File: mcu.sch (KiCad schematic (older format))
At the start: 73 parts, among them J11 RJ45_Shielded, J13 HR911105A, J2 RJ45_Shielded, U3 STM32F207VGT6, U4 MCP2562-E-P, U5 LAN8720A, Y1 Crystal_GND24

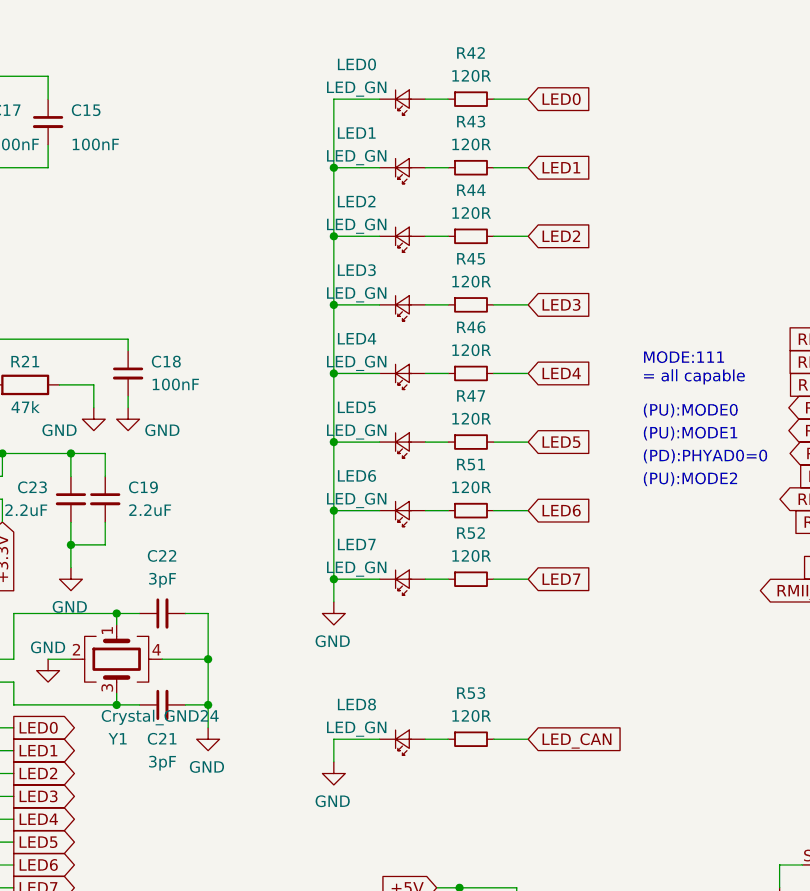
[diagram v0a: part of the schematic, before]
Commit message: added BOM info, minor tweaks to artwork
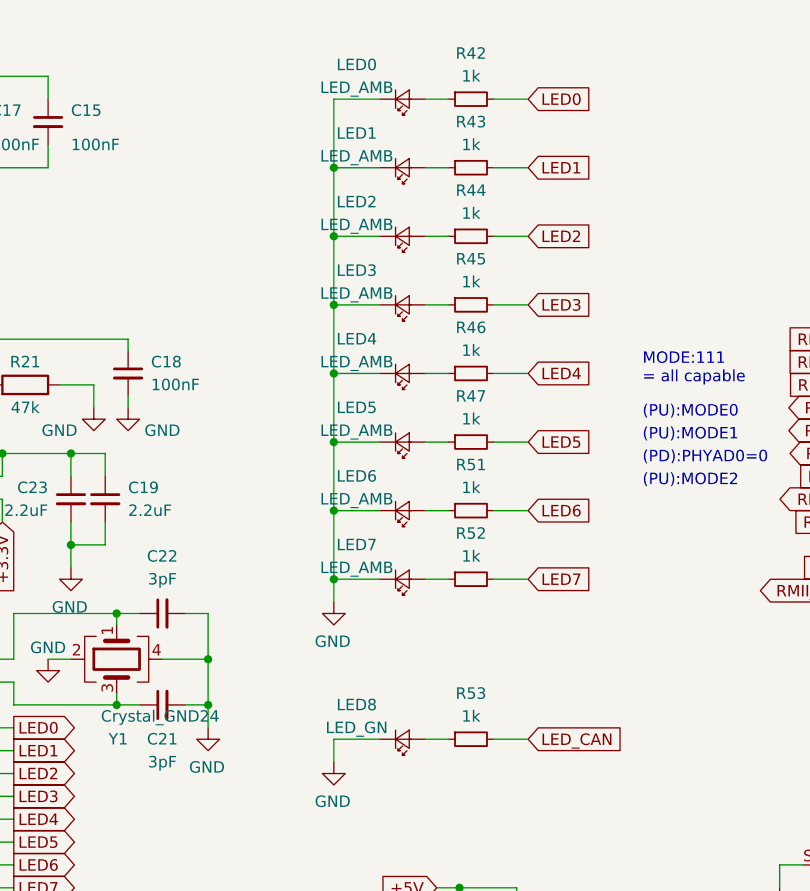
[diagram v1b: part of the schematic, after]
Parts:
- LED0: value LED_GN -> LED_AMB; MPN (none) -> LTST-C190AKT; Mouser (none) -> 859-LTST-C190AKT
- LED1, LED2, LED3, LED4, LED5, LED6, LED7: value LED_GN -> LED_AMB
- R42, R43, R44, R45, R46, R47, R51, R52, R53: value 120R -> 1k
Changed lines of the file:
@@
 P 5250 950
 F 0 "LED0" H 5050 800 50  0000 C CNN
-F 1 "LED_GN" H 5050 900 50  0000 C CNN
+F 1 "LED_AMB" H 5050 900 50  0000 C CNN
 F 2 "LED_SMD:LED_0603_1608Metric_Castellated" V 5250 950 50  0001 C CNN
 F 3 "~" V 5250 950 50  0001 C CNN
+F 4 "LTST-C190AKT" H 5250 950 50  0001 C CNN "MPN"
+F 5 "859-LTST-C190AKT" H 5250 950 50  0001 C CNN "Mouser"
 	1    5250 950
 	1    0    0    1
@@
 AR Path="/5C211FC6/5BE6601F" Ref="R?"  Part="1"
 F 0 "R42" V 5350 950 50  0000 C CNN
-F 1 "120R" V 5450 950 50  0000 C CNN
+F 1 "1k" V 5450 950 50  0000 C CNN
 F 2 "Resistor_SMD:R_0603_1608Metric" H 5550 950 50  0001 C CNN
 F 3 "~" H 5550 950 50  0001 C CNN
@@
 P 5250 1250
 F 0 "LED1" H 5050 1100 50  0000 C CNN
-F 1 "LED_GN" H 5050 1200 50  0000 C CNN
+F 1 "LED_AMB" H 5050 1200 50  0000 C CNN
 F 2 "LED_SMD:LED_0603_1608Metric_Castellated" V 5250 1250 50  0001 C CNN
 F 3 "~" V 5250 1250 50  0001 C CNN
@@
 AR Path="/5C211FC6/5C0171BB" Ref="R?"  Part="1"
 F 0 "R43" V 5350 1250 50  0000 C CNN
-F 1 "120R" V 5450 1250 50  0000 C CNN
+F 1 "1k" V 5450 1250 50  0000 C CNN
 F 2 "Resistor_SMD:R_0603_1608Metric" H 5550 1250 50  0001 C CNN
 F 3 "~" H 5550 1250 50  0001 C CNN
@@
 P 5250 1550
 F 0 "LED2" H 5050 1400 50  0000 C CNN
-F 1 "LED_GN" H 5050 1500 50  0000 C CNN
+F 1 "LED_AMB" H 5050 1500 50  0000 C CNN
 F 2 "LED_SMD:LED_0603_1608Metric_Castellated" V 5250 1550 50  0001 C CNN
 F 3 "~" V 5250 1550 50  0001 C CNN
@@
 AR Path="/5C211FC6/5C036412" Ref="R?"  Part="1"
 F 0 "R44" V 5350 1550 50  0000 C CNN
-F 1 "120R" V 5450 1550 50  0000 C CNN
+F 1 "1k" V 5450 1550 50  0000 C CNN
 F 2 "Resistor_SMD:R_0603_1608Metric" H 5550 1550 50  0001 C CNN
 F 3 "~" H 5550 1550 50  0001 C CNN
@@
 P 5250 1850
 F 0 "LED3" H 5050 1700 50  0000 C CNN
-F 1 "LED_GN" H 5050 1800 50  0000 C CNN
+F 1 "LED_AMB" H 5050 1800 50  0000 C CNN
 F 2 "LED_SMD:LED_0603_1608Metric_Castellated" V 5250 1850 50  0001 C CNN
 F 3 "~" V 5250 1850 50  0001 C CNN
@@
 AR Path="/5C211FC6/5C05605C" Ref="R?"  Part="1"
 F 0 "R45" V 5350 1850 50  0000 C CNN
-F 1 "120R" V 5450 1850 50  0000 C CNN
+F 1 "1k" V 5450 1850 50  0000 C CNN
 F 2 "Resistor_SMD:R_0603_1608Metric" H 5550 1850 50  0001 C CNN
 F 3 "~" H 5550 1850 50  0001 C CNN
@@
 P 5250 2150
 F 0 "LED4" H 5050 2000 50  0000 C CNN
-F 1 "LED_GN" H 5050 2100 50  0000 C CNN
+F 1 "LED_AMB" H 5050 2100 50  0000 C CNN
 F 2 "LED_SMD:LED_0603_1608Metric_Castellated" V 5250 2150 50  0001 C CNN
 F 3 "~" V 5250 2150 50  0001 C CNN
@@
 AR Path="/5C211FC6/5C0760E4" Ref="R?"  Part="1"
 F 0 "R46" V 5350 2150 50  0000 C CNN
-F 1 "120R" V 5450 2150 50  0000 C CNN
+F 1 "1k" V 5450 2150 50  0000 C CNN
 F 2 "Resistor_SMD:R_0603_1608Metric" H 5550 2150 50  0001 C CNN
 F 3 "~" H 5550 2150 50  0001 C CNN
@@
 P 5250 2450
 F 0 "LED5" H 5050 2300 50  0000 C CNN
-F 1 "LED_GN" H 5050 2400 50  0000 C CNN
+F 1 "LED_AMB" H 5050 2400 50  0000 C CNN
 F 2 "LED_SMD:LED_0603_1608Metric_Castellated" V 5250 2450 50  0001 C CNN
 F 3 "~" V 5250 2450 50  0001 C CNN
@@
 AR Path="/5C211FC6/5C0960DF" Ref="R?"  Part="1"
 F 0 "R47" V 5350 2450 50  0000 C CNN
-F 1 "120R" V 5450 2450 50  0000 C CNN
+F 1 "1k" V 5450 2450 50  0000 C CNN
 F 2 "Resistor_SMD:R_0603_1608Metric" H 5550 2450 50  0001 C CNN
 F 3 "~" H 5550 2450 50  0001 C CNN
@@
 P 5250 2750
 F 0 "LED6" H 5050 2600 50  0000 C CNN
-F 1 "LED_GN" H 5050 2700 50  0000 C CNN
+F 1 "LED_AMB" H 5050 2700 50  0000 C CNN
 F 2 "LED_SMD:LED_0603_1608Metric_Castellated" V 5250 2750 50  0001 C CNN
 F 3 "~" V 5250 2750 50  0001 C CNN
@@
 AR Path="/5C211FC6/5C0B676E" Ref="R?"  Part="1"
 F 0 "R51" V 5350 2750 50  0000 C CNN
-F 1 "120R" V 5450 2750 50  0000 C CNN
+F 1 "1k" V 5450 2750 50  0000 C CNN
 F 2 "Resistor_SMD:R_0603_1608Metric" H 5550 2750 50  0001 C CNN
 F 3 "~" H 5550 2750 50  0001 C CNN
@@
 P 5250 3050
 F 0 "LED7" H 5050 2900 50  0000 C CNN
-F 1 "LED_GN" H 5050 3000 50  0000 C CNN
+F 1 "LED_AMB" H 5050 3000 50  0000 C CNN
 F 2 "LED_SMD:LED_0603_1608Metric_Castellated" V 5250 3050 50  0001 C CNN
 F 3 "~" V 5250 3050 50  0001 C CNN
@@
 AR Path="/5C211FC6/5C12EE79" Ref="R?"  Part="1"
 F 0 "R52" V 5350 3050 50  0000 C CNN
-F 1 "120R" V 5450 3050 50  0000 C CNN
+F 1 "1k" V 5450 3050 50  0000 C CNN
 F 2 "Resistor_SMD:R_0603_1608Metric" H 5550 3050 50  0001 C CNN
 F 3 "~" H 5550 3050 50  0001 C CNN
@@
 AR Path="/5C211FC6/5C152FC5" Ref="R?"  Part="1"
 F 0 "R53" V 5350 3750 50  0000 C CNN
-F 1 "120R" V 5450 3750 50  0000 C CNN
+F 1 "1k" V 5450 3750 50  0000 C CNN
 F 2 "Resistor_SMD:R_0603_1608Metric" H 5550 3750 50  0001 C CNN
 F 3 "~" H 5550 3750 50  0001 C CNN

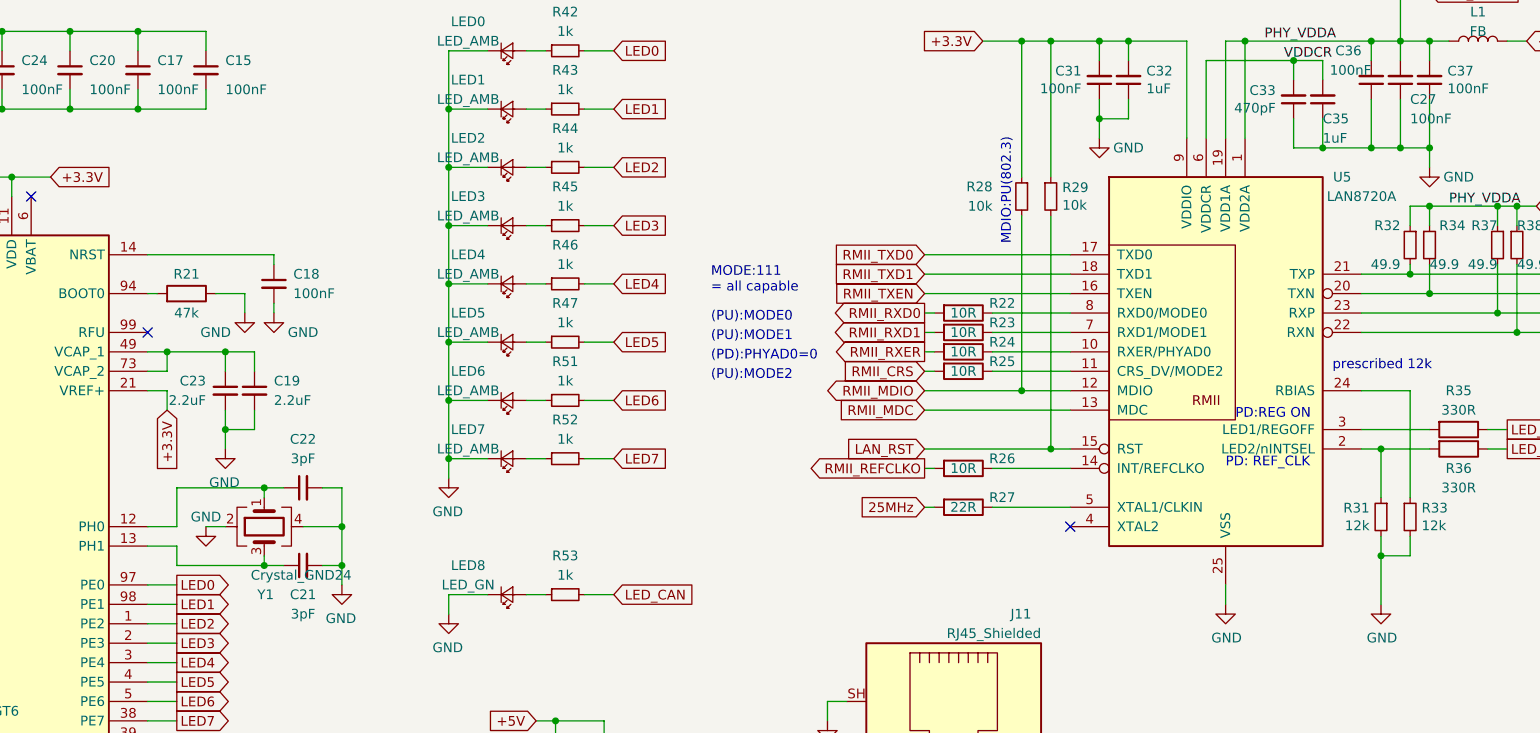
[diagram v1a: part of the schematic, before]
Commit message: adds reset button, some xtal guarding. Schematic reviewed in this version, see https://hackmd.io/-iUjavK_Rz-11sfgLlTnuA# - xtal could be swapped for C_L 10 pF version to reduce susceptibility to environmental factors.
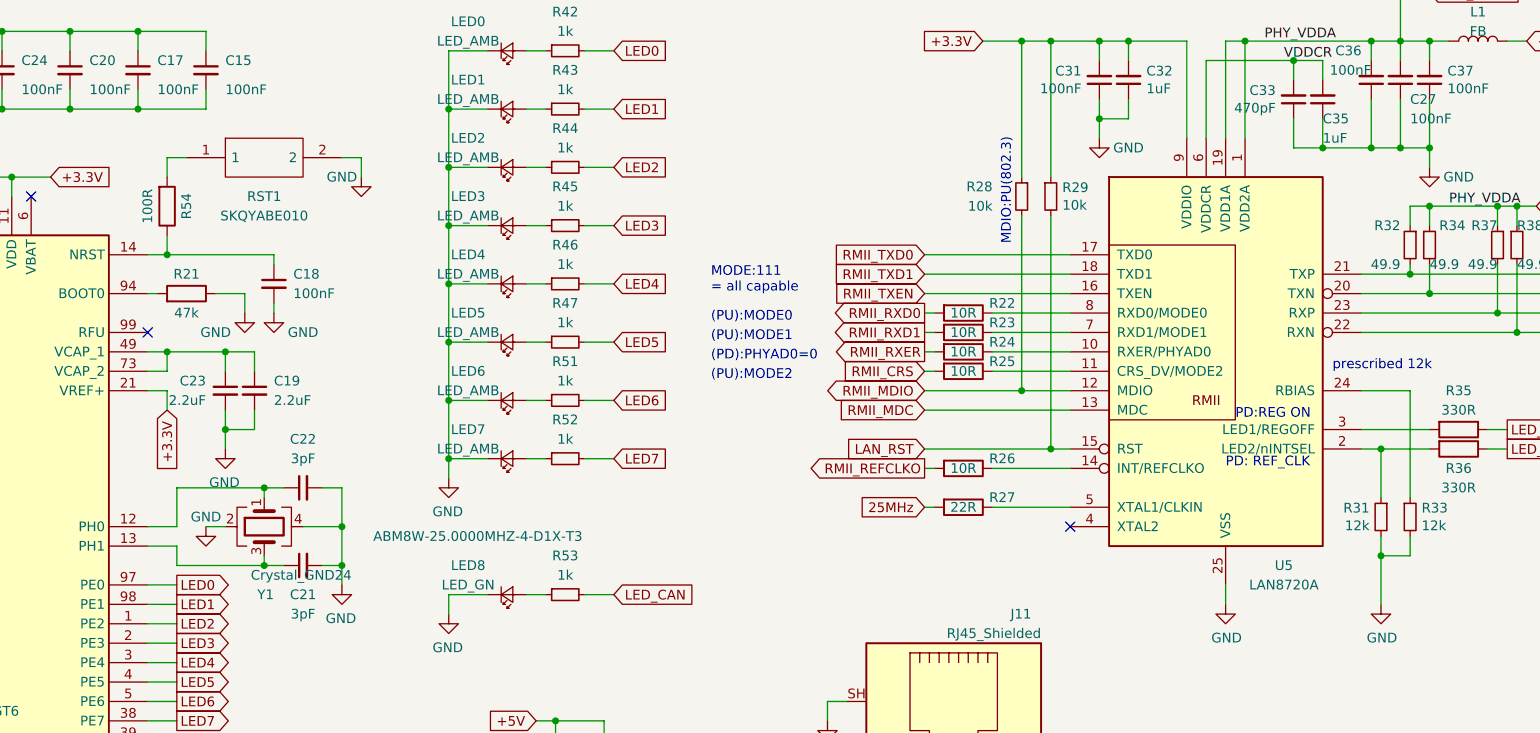
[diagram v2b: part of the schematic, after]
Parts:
- added R54: 100R, Resistor_SMD:R_0603_1608Metric, symbol Device:R
- added RST1: SKQYABE010, SamacSys_Parts:SKQYABE010, symbol SamacSys_Parts:SKQYABE010
- Y1: MPN ABM8-25.000MHZ-10-D1G-T -> ABM8W-25.0000MHZ-4-D1X-T3; Mouser 815-ABM8-25-10-D1G-T -> 815-8W25-4D1XT
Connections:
- net GND: now also RST1.2
- net at C18.1, U3.14 (NRST): now also R54.1
- new net: R54.2, RST1.1
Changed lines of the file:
@@
 AR Path="/5C211DD3/5BBD20DE" Ref="U?"  Part="1"
 AR Path="/5C211FC6/5BBD20DE" Ref="U?"  Part="1"
-F 0 "U5" H 9550 3600 50  0000 C CNN
-F 1 "LAN8720A" H 9650 3500 50  0000 C CNN
+F 0 "U5" H 9250 1600 50  0000 C CNN
+F 1 "LAN8720A" H 9250 1500 50  0000 C CNN
 F 2 "Package_DFN_QFN:QFN-24-1EP_4x4mm_P0.5mm_EP2.6x2.6mm" H 9000 1650 50  0001 L CNN
 F 3 "http://ww1.microchip.com/downloads/en/DeviceDoc/8720a.pdf" H 8750 1650 50  0001 C CNN
@@
 F 2 "Crystal:Crystal_SMD_Abracon_ABM8G-4Pin_3.2x2.5mm" H 4000 3400 50  0001 C CNN
 F 3 "~" H 4000 3400 50  0001 C CNN
-F 4 "ABM8-25.000MHZ-10-D1G-T " V 4000 3400 50  0001 C CNN "MPN"
-F 5 "815-ABM8-25-10-D1G-T " V 4000 3400 50  0001 C CNN "Mouser"
+F 4 "ABM8W-25.0000MHZ-4-D1X-T3" V 4050 2300 50  0000 C CNN "MPN"
+F 5 "815-8W25-4D1XT" V 4000 3400 50  0001 C CNN "Mouser"
 	1    4000 3400
 	0    -1   1    0
@@
 $EndComp
 Wire Wire Line
-	3400 2000 4050 2000
+	3400 2000 3500 2000
 Wire Wire Line
 	4000 3600 4100 3600
@@
 Wire Wire Line
 	9750 5850 9750 5750
+$Comp
+L SamacSys_Parts:SKQYABE010 RST1
+U 1 1 5BE29C94
+P 3600 1500
+F 0 "RST1" H 4000 1300 50  0000 C CNN
+F 1 "SKQYABE010" H 4000 1200 50  0000 C CNN
+F 2 "SamacSys_Parts:SKQYABE010" H 4250 1600 50  0001 L CNN
+F 3 "http://www.alps.com/prod/info/E/HTML/Tact/SurfaceMount/SKQY/SKQYABE010.html#Dimensions" H 4250 1500 50  0001 L CNN
+F 4 "Switch Tactile 6.1 x 3.7 SMT 2.55N Black Button Tactile Switch, SPST-NO 50 mA Surface Mount" H 4250 1400 50  0001 L CNN "Description"
+F 5 "2" H 4250 1300 50  0001 L CNN "Height"
+F 6 "ALPS" H 4250 1200 50  0001 L CNN "Manufacturer_Name"
+F 7 "SKQYABE010" H 4250 1100 50  0001 L CNN "Manufacturer_Part_Number"
+F 8 "9174188" H 4250 1000 50  0001 L CNN "RS Part Number"
+F 9 "http://uk.rs-online.com/web/p/products/9174188" H 4250 900 50  0001 L CNN "RS Price/Stock"
+F 10 "SKQYABE010" H 4250 800 50  0001 L CNN "Arrow Part Number"
+F 11 "https://www.arrow.com/en/products/skqyabe010/alps-electric" H 4250 700 50  0001 L CNN "Arrow Price/Stock"
+F 12 "SKQYABE010" H 3600 1500 50  0001 C CNN "MPN"
+F 13 "688-SKQYAB" H 3600 1500 50  0001 C CNN "Mouser"
+	1    3600 1500
+	1    0    0    -1
+$EndComp
+Connection ~ 3500 2000
+Wire Wire Line
+	3500 2000 4050 2000
+$Comp
+L power:GND #PWR0133
+U 1 1 5BEA740B
+P 4500 1600
+AR Path="/5BBC4BB7/5BEA740B" Ref="#PWR0133"  Part="1"
+AR Path="/5C1EFDBE/5BEA740B" Ref="#PWR?"  Part="1"
+AR Path="/5C211DD3/5BEA740B" Ref="#PWR?"  Part="1"
+AR Path="/5C211FC6/5BEA740B" Ref="#PWR?"  Part="1"
+F 0 "#PWR0133" H 4500 1350 50  0001 C CNN
+F 1 "GND" H 4600 1600 50  0000 C CNN
+F 2 "" H 4500 1600 50  0001 C CNN
+F 3 "" H 4500 1600 50  0001 C CNN
+	1    4500 1600
+	-1   0    0    -1
+$EndComp
+Wire Wire Line
+	4400 1500 4500 1500
+Wire Wire Line
+	4500 1500 4500 1600
+$Comp
+L Device:R R54
+U 1 1 5BF06B2A
+P 3500 1750
+AR Path="/5BBC4BB7/5BF06B2A" Ref="R54"  Part="1"
+AR Path="/5C1EFDBE/5BF06B2A" Ref="R?"  Part="1"
+AR Path="/5C211DD3/5BF06B2A" Ref="R?"  Part="1"
+AR Path="/5C211FC6/5BF06B2A" Ref="R?"  Part="1"
+F 0 "R54" V 3600 1750 50  0000 C CNN
+F 1 "100R" V 3400 1750 50  0000 C CNN
+F 2 "Resistor_SMD:R_0603_1608Metric" V 3430 1750 50  0001 C CNN
+F 3 "~" H 3500 1750 50  0001 C CNN
+	1    3500 1750
+	1    0    0    1
+$EndComp
+Wire Wire Line
+	3500 1900 3500 2000
+Wire Wire Line
+	3600 1500 3500 1500
+Wire Wire Line
+	3500 1500 3500 1600
 $EndSCHEMATC
